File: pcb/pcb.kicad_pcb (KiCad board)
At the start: 2 copper layers, 103.5 x 77.5 mm, 30 parts, among them J1 Screw_Terminal_01x03, J2 PWR_IN, J3 Screw_Terminal_01x03, J4 Screw_Terminal_01x03, J5 Screw_Terminal_01x03, J6 Screw_Terminal_01x03, J7 Screw_Terminal_01x03, J8 RELE_OUT, J9 PWR_IN_RELE, K2 SANYOU_SRD_Form_C, Q1 2N3904, U1 ESP32-DEVKITC, U2 PC817

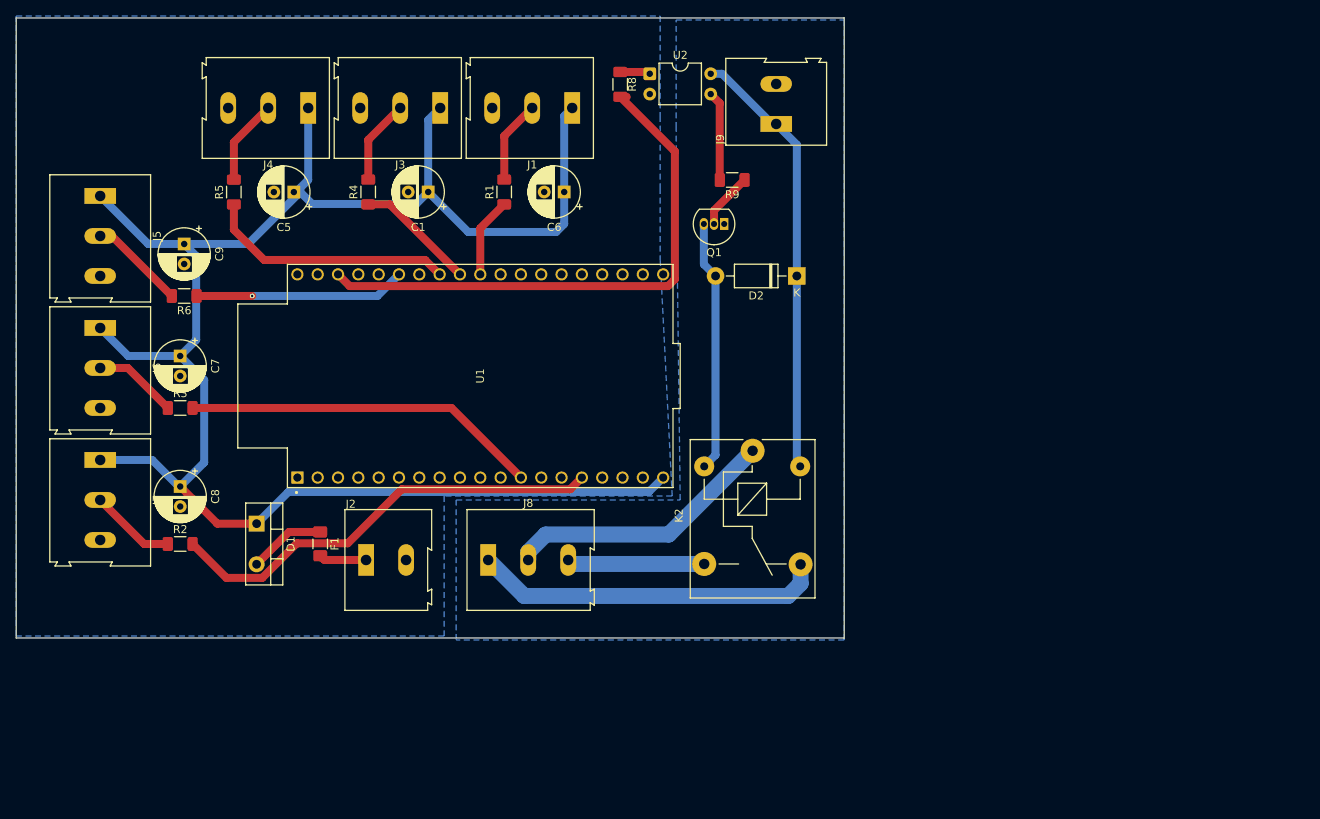
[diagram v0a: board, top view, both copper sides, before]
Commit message: refactor: optimize power efficiency and reduce PCB footprint
Replace series protection diode with P-Channel MOSFET (AOD4185) to minimize voltage drop.

Migrate from ESP32-DevKitC to Wemos D1 Mini (ESP8266) for cost and size reduction.

Replace mechanical relay with N-Channel MOSFET for silent and efficient buzzer control.

Update schematics and PCB layout accordingly.
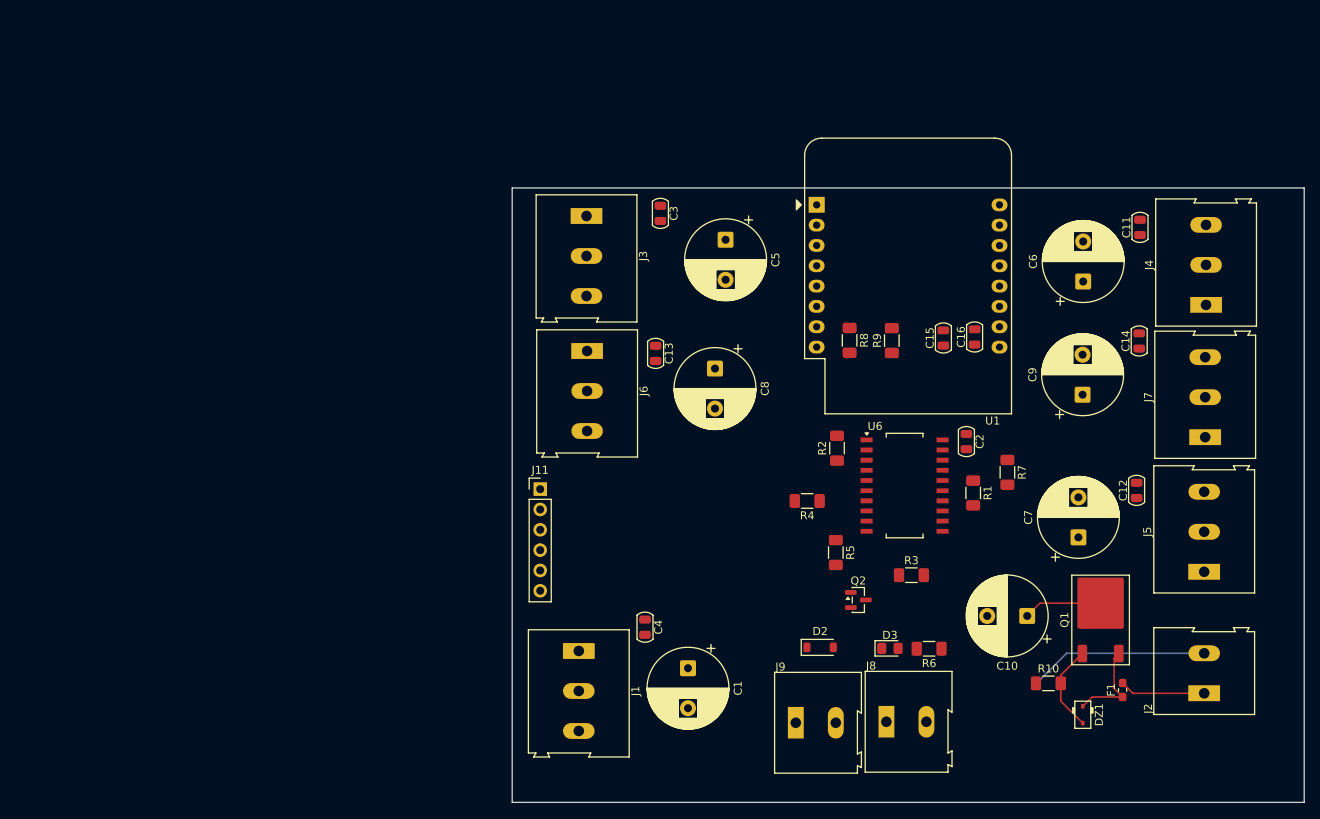
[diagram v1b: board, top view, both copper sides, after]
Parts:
- removed D1: MBR1045, Package_TO_SOT_THT:TO-220-2_Vertical
- removed K2: SANYOU_SRD_Form_C, Relay_THT:Relay_SPDT_SANYOU_SRD_Series_Form_C
- removed U2: PC817, Package_DIP:DIP-4_W7.62mm
- added C10: 16V 2200uf, Capacitor_THT:CP_Radial_D10.0mm_P5.00mm, F.Cu at (153.4, 101.0)
- added C11: 0.1uf, PCM_Capacitor_SMD_AKL:C_0805_2012Metric, F.Cu at (167.5, 52.4)
- added C12: 0.1uf, PCM_Capacitor_SMD_AKL:C_0805_2012Metric, F.Cu at (167.1, 85.3)
- added C13: 0.1uf, PCM_Capacitor_SMD_AKL:C_0805_2012Metric, F.Cu at (106.9, 68.2)
- added C14: 0.1uf, PCM_Capacitor_SMD_AKL:C_0805_2012Metric, F.Cu at (167.4, 66.6)
- added C15: 10uf, PCM_Capacitor_SMD_AKL:C_0805_2012Metric, F.Cu at (142.9, 66.2)
- added C16: 0.1uf, PCM_Capacitor_SMD_AKL:C_0805_2012Metric, F.Cu at (146.8, 66.1)
- added C2: 0.1uf, PCM_Capacitor_SMD_AKL:C_0805_2012Metric, F.Cu at (145.8, 79.2)
- added C3: 0.1uf, PCM_Capacitor_SMD_AKL:C_0805_2012Metric, F.Cu at (107.5, 50.7)
- added C4: 0.1uf, PCM_Capacitor_SMD_AKL:C_0805_2012Metric, F.Cu at (105.6, 102.4)
- added D3: LED, LED_SMD:LED_0805_2012Metric_Pad1.15x1.40mm_HandSolder, F.Cu at (136.2, 105.0)
- added DZ1: BZT52C12S, PCM_Diode_SMD_AKL:D_SOD-323, F.Cu at (160.3, 113.3)
- added J11: Conn_01x06_Pin, Connector_PinHeader_2.54mm:PinHeader_1x06_P2.54mm_Vertical, F.Cu at (92.5, 85.2)
- added Q2: AO3400A, Package_TO_SOT_SMD:SOT-23, F.Cu at (132.3, 99.0)
- added R10: 100K, Resistor_SMD:R_1206_3216Metric_Pad1.30x1.75mm_HandSolder, F.Cu at (156.0, 109.4)
- added R7: 330, Resistor_SMD:R_1206_3216Metric_Pad1.30x1.75mm_HandSolder, F.Cu at (150.9, 83.0)
- added U6: 74AHCT244, Package_SO:SO-20_12.8x7.5mm_P1.27mm, F.Cu at (138.1, 84.7)
- C1, C5, C6, C7, C8, C9: footprint Capacitor_THT:CP_Radial_D6.3mm_P2.50mm -> Capacitor_THT:CP_Radial_D10.0mm_P5.00mm
- D2: value 1N4007 -> 1N4007w; footprint Diode_THT:D_DO-41_SOD81_P10.16mm_Horizontal -> Diode_SMD:D_SOD-123
- F1: value Fuse -> 10A FAST; footprint Fuse:Fuse_1206_3216Metric_Pad1.42x1.75mm_HandSolder -> Fuse:Fuse_0603_1608Metric_Pad1.05x0.95mm_HandSolder
- J1: value Screw_Terminal_01x03 -> PERIODO
- J2: value PWR_IN -> PWR_5V
- J3: value Screw_Terminal_01x03 -> FALTAS_L
- J4: value Screw_Terminal_01x03 -> FALTAS_V
- J5: value Screw_Terminal_01x03 -> CRONOMETRO
- J6: value Screw_Terminal_01x03 -> PUNTAJE_L
- J7: value Screw_Terminal_01x03 -> PUNTAJE_V
- J8: value RELE_OUT -> BOCINA; footprint TerminalBlock:TerminalBlock_Altech_AK300-3_P5.00mm -> TerminalBlock:TerminalBlock_Altech_AK300-2_P5.00mm
- J9: value PWR_IN_RELE -> PWR_12V
- Q1: value 2N3904 -> AOD4185; footprint Package_TO_SOT_THT:TO-92_Inline -> PCM_Package_TO_SOT_SMD_AKL:TO-252-2
- R6: value 330 -> 1K
- R8: value 470 -> 10K
- U1: value ESP32-DEVKITC -> WEMOS_D1_mini; footprint ESP32-DEVKITC:MODULE_ESP32-DEVKITC -> RF_Module:WEMOS_D1_mini_light
- moved J5 145.8 mm to (175.5, 95.5), turned to 90 degrees
- moved J7 138.2 mm to (175.6, 78.7), turned to 90 degrees
- moved J4 114.9 mm to (175.7, 62.1), turned to 90 degrees
- moved C7 114.5 mm to (159.8, 91.2), turned to 90 degrees
- moved C9 113.9 mm to (160.3, 73.3), turned to 90 degrees
- moved J2 106.1 mm to (175.5, 110.7), turned to 90 degrees
- moved R6 103.0 mm to (141.1, 105.1)
- moved F1 101.9 mm to (165.3, 110.2), turned to 90 degrees
- moved R3 93.8 mm to (138.9, 95.9)
- moved R5 87.7 mm to (129.4, 93.1), turned to -90 degrees
- moved R2 83.0 mm to (129.6, 80.0), turned to 90 degrees
- moved J9 74.9 mm to (124.5, 114.3), turned to 0 degrees
- moved R1 69.7 mm to (146.6, 85.6), turned to -90 degrees
- moved C8 68.5 mm to (114.3, 70.1)
- moved Q1 68.3 mm to (162.6, 101.5), turned to 90 degrees
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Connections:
- D2 pad 1: VCC -> +12V
- F1 pad 1: Net-(D1-A) -> Net-(DZ1-K)
- J1 pad 2: PIN_CRONOMETRO -> /OUT_PERIODO
- J3 pad 2: PIN_FALTAS_VISITANTE -> /OUT_FALTAS_LOCAL
- J4 pad 2: PIN_FALTAS_LOCAL -> /OUT_FALTAS_VISITANTE
- J5 pad 2: PIN_PERIODO -> /OUT_CRONOMETRO
- J6 pad 2: PIN_PUNTAJE_LOCAL -> /OUT_PUNTAJE_LOCAL
- J7 pad 2: PIN_PUNTAJE_VISITANTE -> /OUT_PUNTAJE_VISITANTE
- J8 pad 1: NC -> +12V
- J8 pad 2: COM -> Net-(D2-A)
- J9 pad 1: VCC -> +12V
- J9 pad 2: GNDPWR -> GND
- Q1 pad 1: GNDPWR -> Net-(DZ1-A)
- Q1 pad 2: Net-(Q1-B) -> +5V
- Q1 pad 3: Net-(D2-A) -> Net-(DZ1-K)
- R1 pad 1: Net-(U1-IO5) -> Net-(U6-1Y1)
- R1 pad 2: PIN_CRONOMETRO -> /OUT_FALTAS_LOCAL
- R2 pad 1: PIN_PUNTAJE_VISITANTE -> Net-(U6-2Y0)
- R2 pad 2: Net-(U1-IO13) -> /OUT_FALTAS_VISITANTE
- R3 pad 1: PIN_PUNTAJE_LOCAL -> Net-(U6-2Y1)
- R3 pad 2: Net-(U1-IO14) -> /OUT_CRONOMETRO
- R4 pad 1: Net-(U1-IO18) -> Net-(U6-2Y2)
- R4 pad 2: PIN_FALTAS_VISITANTE -> /OUT_PUNTAJE_LOCAL
- R5 pad 1: Net-(U1-IO19) -> Net-(U6-2Y3)
- R5 pad 2: PIN_FALTAS_LOCAL -> /OUT_PUNTAJE_VISITANTE
- R6 pad 1: Net-(U1-IO21) -> +12V
- R6 pad 2: PIN_PERIODO -> Net-(D3-A)
- R8 pad 1: Net-(R8-Pad1) -> /PIN_RELAY_BOCINA
- R8 pad 2: PIN_RELAY_BOCINA -> GND
- R9 pad 1: Net-(Q1-B) -> Net-(Q2-G)
- R9 pad 2: Net-(R9-Pad2) -> /PIN_RELAY_BOCINA
- U1 pad 1: unconnected-(U1-3V3-Pad1) -> Net-(J11-Pin_1)
- U1 pad 10: unconnected-(U1-IO26-Pad10) -> GND
- U1 pad 11: unconnected-(U1-IO27-Pad11) -> /D4
- U1 pad 12: Net-(U1-IO14) -> /D3
- U1 pad 13: unconnected-(U1-IO12-Pad13) -> /PIN_FALTAS_VISITANTE
- U1 pad 14: GND -> /PIN_FALTAS_LOCAL
- U1 pad 15: Net-(U1-IO13) -> Net-(J11-Pin_2)
- U1 pad 16: unconnected-(U1-SD2-Pad16) -> Net-(J11-Pin_3)
- U1 pad 2: unconnected-(U1-EN-Pad2) -> /A0
- U1 pad 3: unconnected-(U1-SENSOR_VP-Pad3) -> /PIN_PERIODO
- U1 pad 4: unconnected-(U1-SENSOR_VN-Pad4) -> /PIN_CRONOMETRO
- U1 pad 5: unconnected-(U1-IO34-Pad5) -> /PIN_PUNTAJE_LOCAL
- U1 pad 6: unconnected-(U1-IO35-Pad6) -> /PIN_PUNTAJE_VISITANTE
- U1 pad 7: unconnected-(U1-IO32-Pad7) -> /PIN_RELAY_BOCINA
- U1 pad 9: unconnected-(U1-IO25-Pad9) -> +5V
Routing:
- net +5V: track 225.6 -> 9.84 mm
- net PIN_RELAY_BOCINA: track 69.5 -> 0.00 mm
- net Net-(U1-IO13): track 55.6 -> 0.00 mm
- net VCC: track 54.8 -> 0.00 mm
- net Net-(U1-IO14): track 44.6 -> 0.00 mm
- net NC: track 44.0 -> 0.00 mm
- net COM: track 34.3 -> 0.00 mm
- net Net-(D2-A): track 31.5 -> 0.00 mm
- net Net-(U1-IO19): track 31.2 -> 0.00 mm
- net Net-(U1-IO21): track 26.4 -> 0.00 mm, vias 1 -> 0
- net GND: track 0.00 -> 22.6 mm
- net NO: track 17.2 -> 0.00 mm
- net Net-(U1-IO18): track 15.1 -> 0.00 mm
- net PIN_PERIODO: track 12.1 -> 0.00 mm
- net Net-(DZ1-K): track 0.00 -> 11.6 mm
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- removed copper zone on B.Cu, net GND
- removed copper zone on B.Cu, net GNDPWR
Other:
- board size 103.5 x 77.5 mm -> 99 x 76.8 mm

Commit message: feat(pcb): Actualizar diseño y eliminar esquemático obsoleto
- Reemplaza conector de 6 por 5 pines en el esquemático.

- Regenera el layout del PCB y actualiza el ruteado.

- Añade nuevo ancho de pista de 0.35mm en la configuración.

- Elimina el archivo de esquemático no utilizado 'untitled.kicad_sch'.
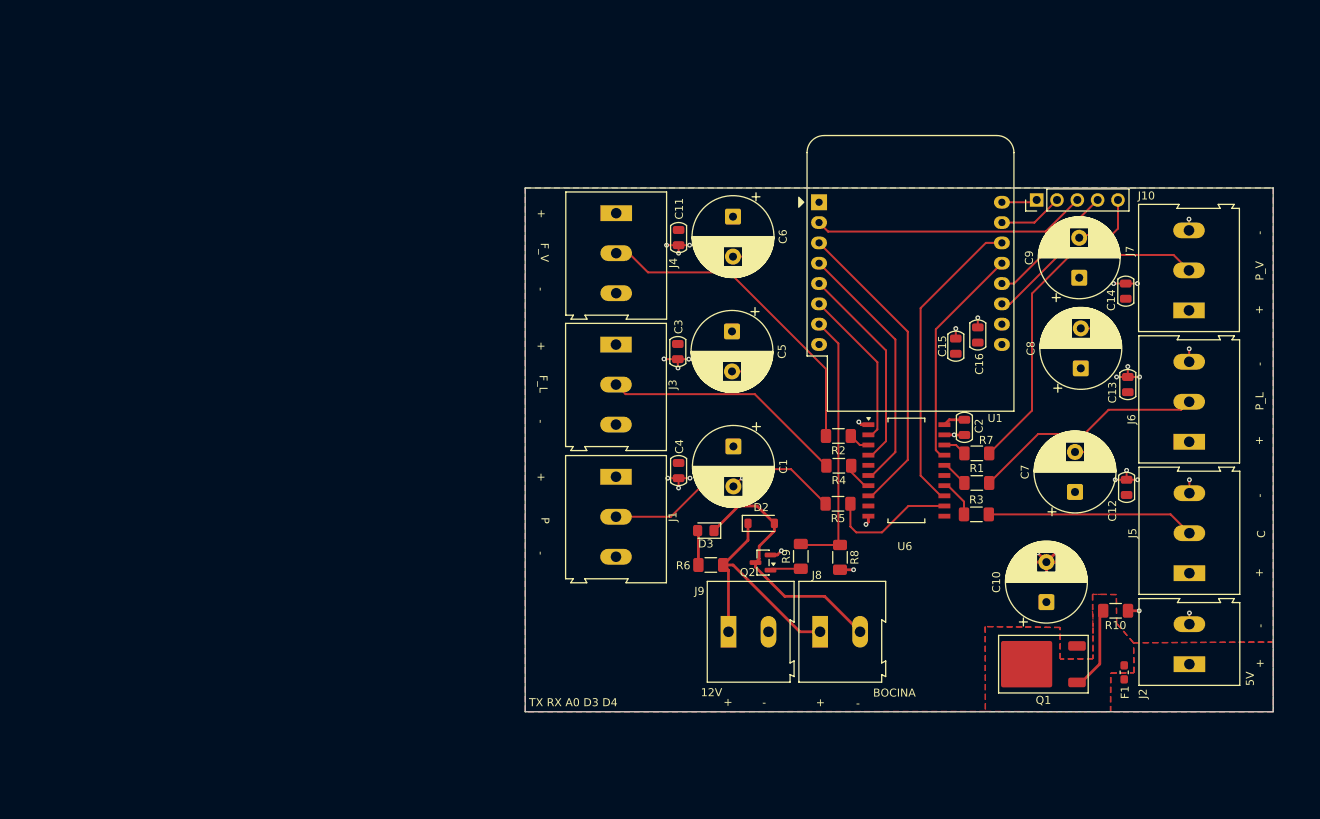
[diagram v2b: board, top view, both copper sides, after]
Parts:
- removed DZ1: BZT52C12S, PCM_Diode_SMD_AKL:D_SOD-323
- removed J11: Conn_01x06_Pin, Connector_PinHeader_2.54mm:PinHeader_1x06_P2.54mm_Vertical
- added J10: Conn_01x05_Pin, Connector_PinHeader_2.54mm:PinHeader_1x05_P2.54mm_Vertical, F.Cu at (154.6, 49.0)
- moved J6 76.1 mm to (173.6, 79.2), turned to 90 degrees
- moved J4 74.6 mm to (102.0, 50.6), turned to -90 degrees
- moved C13 59.2 mm to (165.9, 72.1), turned to 90 degrees
- moved C11 57.7 mm to (109.8, 53.7), turned to -90 degrees
- moved C8 45.7 mm to (160.1, 70.0), turned to 90 degrees
- moved C6 44.5 mm to (116.6, 51.1), turned to -90 degrees
- moved R9 29.3 mm to (125.1, 93.5)
- moved R6 29.2 mm to (113.8, 94.6)
- moved C1 28.3 mm to (116.7, 79.8)
- moved D3 27.3 mm to (113.2, 90.3), turned to 180 degrees
- moved R8 27.2 mm to (130.0, 93.7)
- moved J1 22.3 mm to (102.0, 83.6)
- moved C4 20.0 mm to (109.8, 82.8)
- moved C3 17.4 mm to (109.7, 68.0)
- moved D2 17.2 mm to (120.1, 89.4)
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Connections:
- F1 pad 1: Net-(DZ1-K) -> Net-(Q1-D)
- Q1 pad 2: +5V -> Net-(Q1-D)
- Q1 pad 3: Net-(DZ1-K) -> +5V
- R1 pad 2: /OUT_FALTAS_LOCAL -> /OUT_PUNTAJE_LOCAL
- R3 pad 1: Net-(U6-2Y1) -> Net-(U6-1Y2)
- R4 pad 2: /OUT_PUNTAJE_LOCAL -> /OUT_FALTAS_LOCAL
- R5 pad 1: Net-(U6-2Y3) -> Net-(U6-1Y3)
- R5 pad 2: /OUT_PUNTAJE_VISITANTE -> /OUT_PERIODO
- R7 pad 2: /OUT_PERIODO -> /OUT_PUNTAJE_VISITANTE
- U1 pad 1: Net-(J11-Pin_1) -> unconnected-(U1-~{RST}-Pad1)
- U1 pad 15: Net-(J11-Pin_2) -> /RX
- U1 pad 16: Net-(J11-Pin_3) -> /TX
- U6 pad 11: /PIN_PUNTAJE_VISITANTE -> unconnected-(U6-2A3-Pad11)
- U6 pad 12: unconnected-(U6-1Y3-Pad12) -> Net-(U6-1Y3)
- U6 pad 13: /PIN_PUNTAJE_LOCAL -> /PIN_FALTAS_LOCAL
- U6 pad 14: unconnected-(U6-1Y2-Pad14) -> Net-(U6-1Y2)
- U6 pad 15: /PIN_CRONOMETRO -> unconnected-(U6-2A1-Pad15)
- U6 pad 2: /PIN_PERIODO -> /PIN_PUNTAJE_VISITANTE
- U6 pad 4: /PIN_FALTAS_LOCAL -> /PIN_PUNTAJE_LOCAL
- U6 pad 5: Net-(U6-2Y1) -> unconnected-(U6-2Y1-Pad5)
- U6 pad 6: unconnected-(U6-1A2-Pad6) -> /PIN_CRONOMETRO
- U6 pad 8: unconnected-(U6-1A3-Pad8) -> /PIN_PERIODO
- U6 pad 9: Net-(U6-2Y3) -> unconnected-(U6-2Y3-Pad9)
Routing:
- net /OUT_PUNTAJE_VISITANTE: track 0.00 -> 44.6 mm
- net GND: track 22.6 -> 62.3 mm, vias 0 -> 40
- net /OUT_FALTAS_VISITANTE: track 0.00 -> 39.0 mm
- net /PIN_PERIODO: track 0.00 -> 38.5 mm
- net /PIN_FALTAS_LOCAL: track 0.00 -> 38.5 mm
- net /A0: track 0.00 -> 34.4 mm
- net /PIN_RELAY_BOCINA: track 0.00 -> 33.6 mm
- net Net-(D2-A): track 0.00 -> 32.6 mm
- net /PIN_CRONOMETRO: track 0.00 -> 32.2 mm
- net +12V: track 0.00 -> 30.7 mm
- net /OUT_FALTAS_LOCAL: track 0.00 -> 30.5 mm
- net /OUT_PERIODO: track 0.00 -> 30.5 mm
- net /OUT_PUNTAJE_LOCAL: track 0.00 -> 29.2 mm
- net /PIN_FALTAS_VISITANTE: track 0.00 -> 28.1 mm
- net /PIN_PUNTAJE_LOCAL: track 0.00 -> 26.1 mm
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- added copper zone on F.Cu, net +5V
- added copper zone on B.Cu, net GND
- added copper zone on F.Cu, net Net-(J2-Pin_1)
- added copper zone on F.Cu, net Net-(Q1-D)
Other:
- board size 99 x 76.8 mm -> 93.5 x 65.5 mm
- board text added: "+"
- board text added: "-"
- board text added: "12V"
- board text added: "5V"
- board text added: "BOCINA"
- board text added: "C"
- board text added: "F_L"
- board text added: "F_V"
- board text added: "P"
- board text added: "P_L"
- board text added: "P_V"
- board text added: "TX RX A0 D3 D4"
